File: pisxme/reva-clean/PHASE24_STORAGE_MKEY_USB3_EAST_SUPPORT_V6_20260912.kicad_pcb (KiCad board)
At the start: 6 copper layers, 300 x 180 mm, 131 parts, among them J1 74221-101LF, J2 A70-112-331N126, J3 1-2199230-4, J4 Amphenol 10171746-00021LF USB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, J5 0039300020, J6 0039300020, J7 Raspberry-Pi-5-Compute-Module, Q1 CSD19536KCS, Q2 CSD19536KCS, U1 LM74700QDBVRQ1, U2 LM74700QDBVRQ1, U3 TPSM63606RDLR, U4 TPSM63606RDLR, U5 TPSM63606RDLR, U6 TPD4EUSB30, U7 TUSB9261IPVP, U8 Texas_DRT_3, U9 TPD4EUSB30, Y10 25MHz

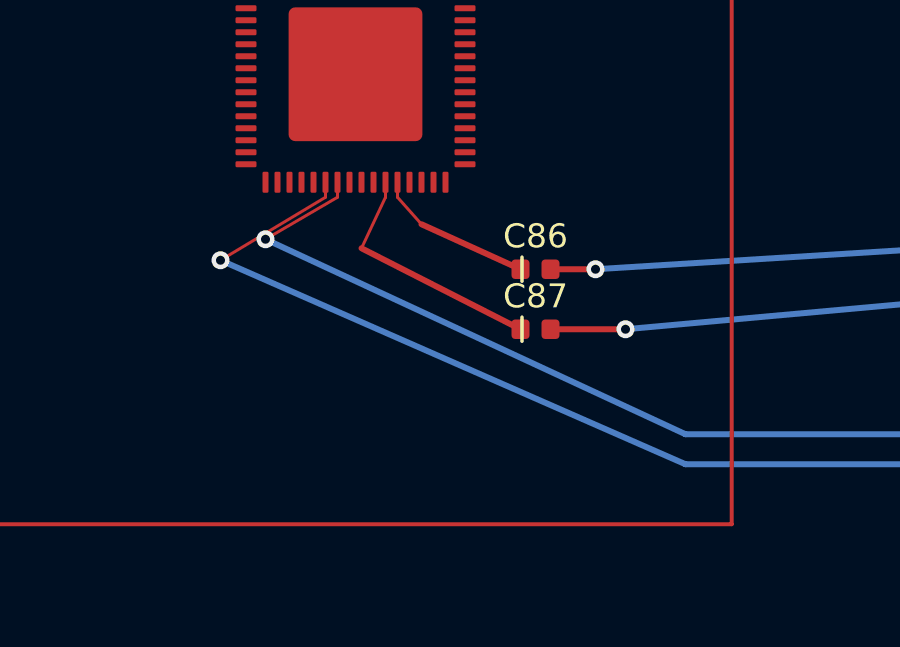
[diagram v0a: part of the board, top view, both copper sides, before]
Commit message: phase24: refine USB3 QFN fanout geometry
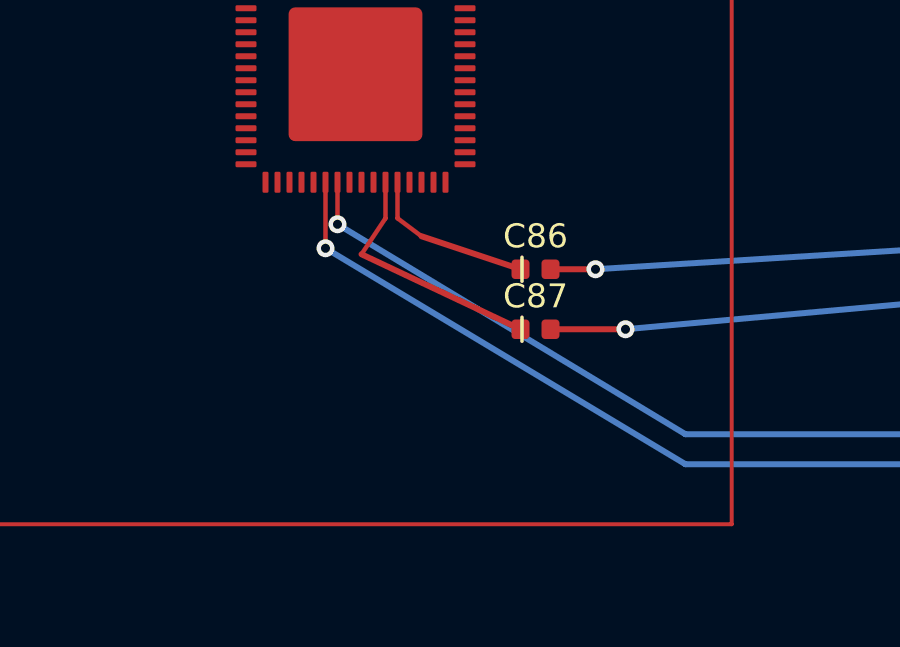
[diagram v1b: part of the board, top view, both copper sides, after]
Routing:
- net USB_RXN1: track 58.2 -> 52.9 mm
- net USB_RXP1: track 54.0 -> 50.3 mm
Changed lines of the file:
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@@
 	(segment
 		(start 139 138.6)
-		(end 139 139.1)
-		(width 0.1)
+		(end 139 140.8)
+		(width 0.15)
 		(layer "F.Cu")
 		(net "USB_RXN1")
@@
 		(net "USB_RXN1")
 	)
-	(segment
-		(start 139 139.1)
-		(end 135.5 141.2)
-		(width 0.1)
-		(layer "F.Cu")
+	(via
+		(at 139 140.8)
+		(size 0.6)
+		(drill 0.3)
+		(layers "F.Cu" "B.Cu")
 		(net "USB_RXN1")
 	)
@@
 		(net "USB_RXN1")
 	)
-	(via
-		(at 135.5 141.2)
-		(size 0.6)
-		(drill 0.3)
-		(layers "F.Cu" "B.Cu")
+	(segment
+		(start 172.5 148)
+		(end 172.5 138.8)
+		(width 0.2)
+		(layer "B.Cu")
+		(net "USB_RXN1")
+	)
+	(segment
+		(start 139 140.8)
+		(end 151 148)
+		(width 0.2)
+		(layer "B.Cu")
 		(net "USB_RXN1")
 	)
@@
 	)
 	(segment
-		(start 172.5 148)
-		(end 172.5 138.8)
-		(width 0.2)
-		(layer "B.Cu")
-		(net "USB_RXN1")
-	)
-	(segment
-		(start 135.5 141.2)
-		(end 151 148)
-		(width 0.2)
-		(layer "B.Cu")
-		(net "USB_RXN1")
-	)
-	(segment
-		(start 139.4 138.6)
-		(end 139.4 139.1)
-		(width 0.1)
-		(layer "F.Cu")
-		(net "USB_RXP1")
-	)
-	(segment
 		(start 171.5 137.2)
 		(end 166.5 137.8)
@@
 	)
 	(segment
-		(start 139.4 139.1)
-		(end 137 140.5)
-		(width 0.1)
-		(layer "F.Cu")
-		(net "USB_RXP1")
-	)
-	(via
-		(at 137 140.5)
-		(size 0.6)
-		(drill 0.3)
-		(layers "F.Cu" "B.Cu")
+		(start 139.4 138.6)
+		(end 139.4 140)
+		(width 0.15)
+		(layer "F.Cu")
 		(net "USB_RXP1")
 	)
@@
 		(net "USB_RXP1")
 	)
+	(via
+		(at 139.4 140)
+		(size 0.6)
+		(drill 0.3)
+		(layers "F.Cu" "B.Cu")
+		(net "USB_RXP1")
+	)
 	(segment
 		(start 151 147)
@@
 	)
 	(segment
-		(start 137 140.5)
+		(start 139.4 140)
 		(end 151 147)
 		(width 0.2)
@@
 	)
 	(segment
+		(start 146.5 143.5)
+		(end 149 143.5)
+		(width 0.2)
+		(layer "F.Cu")
+		(net "JMS_USB3_TXN")
+	)
+	(segment
 		(start 170 136.4)
 		(end 166.5 137.4)
@@
 		(net "JMS_USB3_TXN")
 	)
-	(segment
-		(start 146.5 143.5)
-		(end 149 143.5)
-		(width 0.2)
-		(layer "F.Cu")
-		(net "JMS_USB3_TXN")
-	)
 	(via
 		(at 170 136.4)
@@
 	)
 	(segment
+		(start 169 140.2)
+		(end 169 135.8)
+		(width 0.2)
+		(layer "B.Cu")
+		(net "JMS_USB3_TXP")
+	)
+	(segment
 		(start 148 141.5)
 		(end 169 140.2)
-		(width 0.2)
-		(layer "B.Cu")
-		(net "JMS_USB3_TXP")
-	)
-	(segment
-		(start 169 140.2)
-		(end 169 135.8)
 		(width 0.2)
 		(layer "B.Cu")
@@
 	(segment
 		(start 141.4 138.6)
-		(end 141.4 139.1)
-		(width 0.1)
+		(end 141.4 139.8)
+		(width 0.15)
 		(layer "F.Cu")
 		(net "USB_TXP1")
 	)
 	(segment
-		(start 142.2 140)
+		(start 141.4 139.8)
+		(end 142.2 140.4)
+		(width 0.15)
+		(layer "F.Cu")
+		(net "USB_TXP1")
+	)
+	(segment
+		(start 142.2 140.4)
 		(end 145.5 141.5)
 		(width 0.2)
-		(layer "F.Cu")
-		(net "USB_TXP1")
-	)
-	(segment
-		(start 141.4 139.1)
-		(end 142.2 140)
-		(width 0.1)
 		(layer "F.Cu")
 		(net "USB_TXP1")
@@
 	)
 	(segment
-		(start 141 139.1)
-		(end 140.2 140.8)
-		(width 0.1)
+		(start 141 138.6)
+		(end 141 139.8)
+		(width 0.15)
 		(layer "F.Cu")
 		(net "USB_TXN1")
 	)
 	(segment
-		(start 141 138.6)
-		(end 141 139.1)
-		(width 0.1)
+		(start 140.2 141)
+		(end 145.5 143.5)
+		(width 0.2)
 		(layer "F.Cu")
 		(net "USB_TXN1")
 	)
 	(segment
-		(start 140.2 140.8)
-		(end 145.5 143.5)
-		(width 0.2)
+		(start 141 139.8)
+		(end 140.2 141)
+		(width 0.15)
 		(layer "F.Cu")
 		(net "USB_TXN1")
